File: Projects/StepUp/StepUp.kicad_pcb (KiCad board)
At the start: 4 copper layers, 101 x 81 mm, 149 parts, among them J1 USB_C_Receptacle_USB2.0_16P, J10 Conn_01x02, J11 Conn_01x02, J12 Conn_01x02, J13 Conn_01x02, J14 Conn_02x03_Odd_Even, J2 Conn_01x02, J3 Conn_02x03_Odd_Even, J4 Conn_02x06_Odd_Even, J5 Conn_01x01_Pin, J6 Conn_01x01_Pin, J7 TBLH10-350-04BK, J8 Conn_01x01_Pin, J9 Conn_01x02, Q1 BSS84, Q2 2N7002, Q3 PMF170XP,115, Q4 BSS83P, Q5 BSS83P, SW1 FSM8JSMASTR, SW2 FSM8JSMASTR, SW3 FSM8JSMASTR, U1 USBLC6-2SC6, U2 W25Q128JVS, U3 RP2040, U4 TMC2300-LA, U5 NCP1117-3.3_SOT223, U6 MCP73832T-2ACI_OT, U7 MIC2253, Y1 ABM8-272-T3

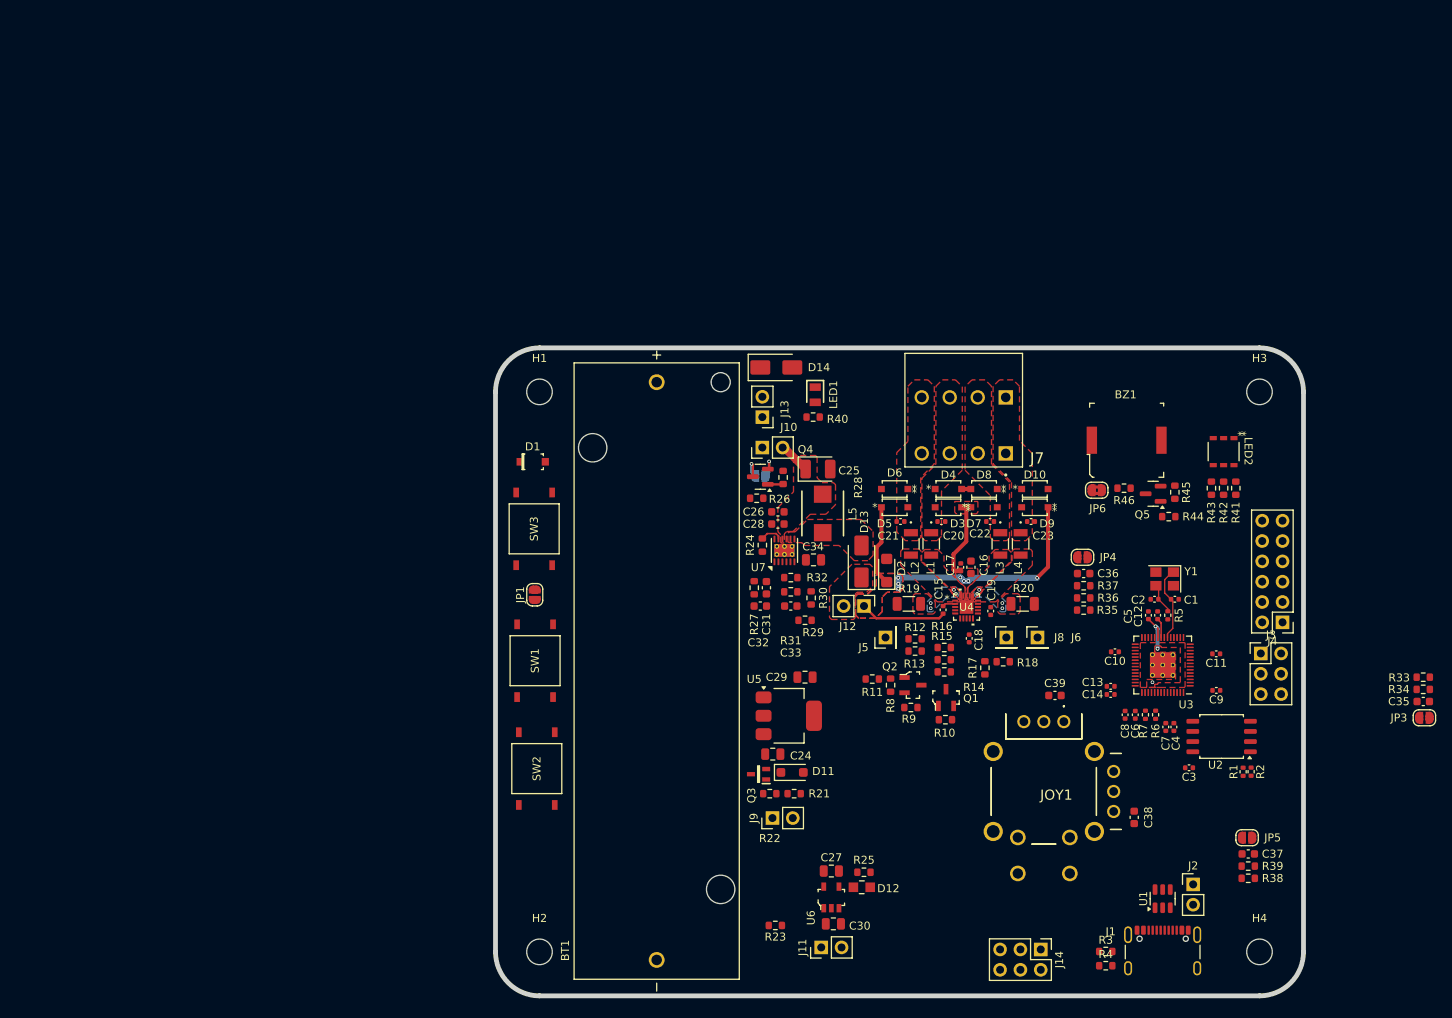
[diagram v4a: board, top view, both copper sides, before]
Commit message: feat(layout): DRC ongoing, layout nearly complete
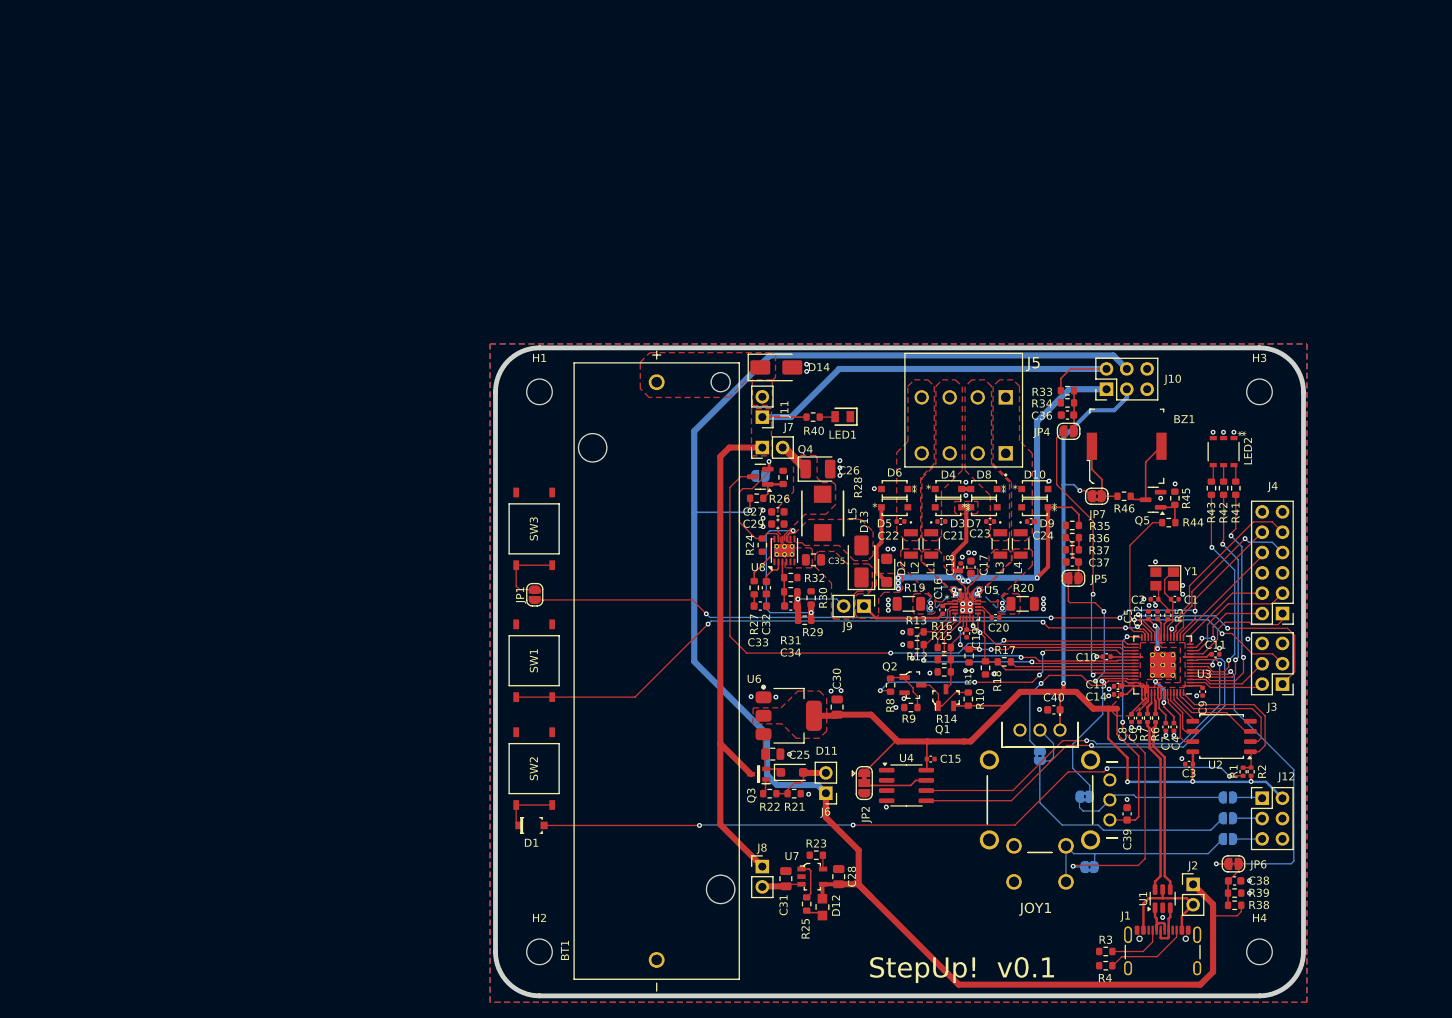
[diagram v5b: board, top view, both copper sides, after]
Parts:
- removed the J5 at (133.2, 100.7)
- removed the J6 at (152.2, 100.7)
- removed the J8 at (148.3, 100.7)
- added C15: 100n, Capacitor_SMD:C_0402_1005Metric, F.Cu at (138.9, 115.9)
- added J10: Conn_02x03_Odd_Even, Connector_PinHeader_2.54mm:PinHeader_2x03_P2.54mm_Vertical, F.Cu at (160.9, 69.7)
- added JP10: SolderJumper_2_Open, Jumper:SolderJumper-2_P1.3mm_Open_RoundedPad1.0x1.5mm, B.Cu at (176.1, 120.7)
- added JP11: SolderJumper_2_Open, Jumper:SolderJumper-2_P1.3mm_Open_RoundedPad1.0x1.5mm, B.Cu at (176.1, 123.3)
- added JP12: SolderJumper_2_Open, Jumper:SolderJumper-2_P1.3mm_Open_RoundedPad1.0x1.5mm, B.Cu at (176.1, 125.9)
- added JP13: SolderJumper_2_Bridged, Jumper:SolderJumper-2_P1.3mm_Bridged2Bar_RoundedPad1.0x1.5mm, B.Cu at (158.8, 129.4)
- added JP2: SolderJumper_3_Open, Jumper:SolderJumper-3_P1.3mm_Bridged12_RoundedPad1.0x1.5mm, F.Cu at (130.6, 118.9)
- added JP8: SolderJumper_2_Bridged, Jumper:SolderJumper-2_P1.3mm_Bridged2Bar_RoundedPad1.0x1.5mm, B.Cu at (152.6, 115.5)
- added JP9: SolderJumper_2_Bridged, Jumper:SolderJumper-2_P1.3mm_Bridged2Bar_RoundedPad1.0x1.5mm, B.Cu at (158.2, 120.6)
- added U4: FM24CL16B, Package_SO:SOIC-8_3.9x4.9mm_P1.27mm, F.Cu at (135.9, 119.2)
- moved C36 57.1 mm to (156.0, 72.9)
- moved JP4 57.1 mm to (156.1, 74.9)
- moved R33 57.1 mm to (156.0, 69.9)
- moved R34 57.1 mm to (156.0, 71.4)
- moved D1 45.5 mm to (89.0, 124.2)
- moved J12 33.5 mm to (180.3, 120.8), turned to 0 degrees
- moved J8 12.5 mm to (117.9, 129.3), turned to 0 degrees
- moved R11 12.4 mm to (143.7, 103.0), turned to -90 degrees
- moved R35 10.7 mm to (156.6, 86.7), turned to 0 degrees
- moved R23 10.2 mm to (124.6, 127.9), turned to 0 degrees
- moved C31 8.19 mm to (120.8, 130.9), turned to 90 degrees
- moved R25 8.19 mm to (123.4, 134.0), turned to -90 degrees
- moved R36 7.67 mm to (156.6, 88.2), turned to 0 degrees
- moved J6 7.36 mm to (125.8, 120.2), turned to 180 degrees
- moved D12 5.51 mm to (125.4, 134.4), turned to -90 degrees
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- renumbered C15 to C16, C16 to C17, C17 to C18, C18 to C19, C19 to C20, C20 to C21, C21 to C22, C22 to C23, C23 to C24, C24 to C25, C25 to C26, C26 to C27, C27 to C28, C28 to C29, C29 to C30, C30 to C31, C31 to C32, C32 to C33, C33 to C34, C34 to C35, C35 to C36, C36 to C37, C37 to C38, C38 to C39, C39 to C40, J13 to J11, J14 to J12, J7 to J5, J9 to J6, J10 to J7, J11 to J8, J12 to J9, JP2 to JP3, JP3 to JP4, JP4 to JP5, JP5 to JP6, JP6 to JP7, U4 to U5, U5 to U6, U6 to U7, U7 to U8
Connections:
- J12 pad 1: JOYSTSICK_AXIS_V -> Net-(J12-Pin_1)
- J12 pad 3: JOYSTSICK_AXIS_H -> Net-(J12-Pin_3)
- J12 pad 5: JOYSTSICK_BUTTON -> Net-(J12-Pin_5)
- J4 pad 1: /MCU/GPIO6 -> /MCU/GPIO8
- J4 pad 10: GND -> /MCU/GPIO13
- J4 pad 3: /MCU/GPIO7 -> /MCU/GPIO9
- J4 pad 5: /MCU/GPIO8 -> GND
- J4 pad 6: /MCU/GPIO12 -> GND
- J4 pad 7: /MCU/GPIO9 -> /MCU/GPIO14
- J4 pad 8: /MCU/GPIO13 -> /MCU/GPIO12
- J4 pad 9: /MCU/GPIO16 -> /MCU/GPIO15
- JOY1 pad 12: JOYSTSICK_AXIS_V -> /User Input/JOYSTICK_AXIS_V
- JOY1 pad 2: JOYSTSICK_AXIS_H -> /User Input/JOYSTICK_AXIS_H
- JOY1 pad B1: JOYSTSICK_BUTTON -> /User Input/JOYSTICK_BUTTON
- JOY1 pad D1: JOYSTSICK_BUTTON -> /User Input/JOYSTICK_BUTTON
- U3 pad 17: TMC_EN -> /MCU/GPIO14
- U3 pad 18: ~{TMC_STBDY} -> /MCU/GPIO15
- U3 pad 27: /MCU/GPIO16 -> BUZZER
- U3 pad 28: BUZZER -> JOY_MCU_BTN
- U3 pad 29: VUSB_MONITOR -> MCU_BOOST_EN
- U3 pad 30: MCU_BOOST_EN -> TMC_DIAG
- U3 pad 31: TMC_DIAG -> TMC_EN
- U3 pad 32: VUSB_MONITOR -> ~{TMC_STBDY}
- U3 pad 34: JOYSTSICK_BUTTON -> TMC_DIR
- U3 pad 35: LED_RED -> TMC_STEP
- U3 pad 36: LED_GREEN -> TMC_UART_TX
- U3 pad 37: LED_BLUE -> TMC_UART_RX
- U3 pad 38: JOYSTSICK_AXIS_V -> VBAT_MONITOR
- U3 pad 39: JOYSTSICK_AXIS_H -> VMOTOR_MONITOR
- U3 pad 4: TMC_STEP -> LED_RED
- U3 pad 40: VBAT_MONITOR -> JOY_AXIS_MCU_V
- U3 pad 41: VMOTOR_MONITOR -> JOY_AXIS_MCU_H
- U3 pad 5: TMC_DIR -> LED_GREEN
- U3 pad 6: TMC_UART_TX -> VUSB_MONITOR
- U3 pad 7: TMC_UART_RX -> LED_BLUE
- U3 pad 8: /MCU/GPIO6 -> /MCU/EEPROM_SDA
- U3 pad 9: /MCU/GPIO7 -> /MCU/EEPROM_SCL
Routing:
- net V_USB: track 0.00 -> 210.5 mm, vias 0 -> 1
- net +3V3: track 2.48 -> 196.0 mm, vias 0 -> 5
- net Vbat: track 0.00 -> 123.3 mm
- net /MCU/GPIO13: track 0.00 -> 101.5 mm, vias 0 -> 4
- net /MCU/~{USB_BOOT}: track 0.00 -> 90.9 mm, vias 0 -> 4
- net /MCU/RUN: track 0.00 -> 84.1 mm, vias 0 -> 4
- net MCU_BOOST_EN: track 3.52 -> 74.5 mm, vias 1 -> 2
- net /MCU/EEPROM_SDA: track 0.00 -> 53.3 mm, vias 0 -> 2
- net /MCU/EEPROM_SCL: track 0.00 -> 50.5 mm, vias 0 -> 2
- net VUSB_MONITOR: track 0.00 -> 43.8 mm, vias 0 -> 2
- net JOY_MCU_BTN: track 0.00 -> 42.1 mm, vias 0 -> 3
- net VBAT_MONITOR: track 0.00 -> 38.2 mm, vias 0 -> 2
- net TMC_DIR: track 0.00 -> 38.1 mm, vias 0 -> 2
- net ~{TMC_STBDY}: track 0.00 -> 36.9 mm, vias 0 -> 4
- net /User Input/JOYSTICK_AXIS_H: track 0.00 -> 35.8 mm
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- added copper zone on B.Cu, net GND
- added copper zone on F.Cu, net GND
- added copper zone on F.Cu, net Net-(D14-K)
- added copper zone on F.Cu, net Vbat
- removed copper zone on B.Cu, net VMotor
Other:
- board text added: "StepUp! v0.1"

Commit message: feat(StepUp): Release v0.1
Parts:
- added R8: 10kR, Resistor_SMD:R_0603_1608Metric, F.Cu at (82.4, 78.1)
- added R9: 10kR, Resistor_SMD:R_0603_1608Metric, F.Cu at (84.6, 79.3)
- C1, C2: value 15p -> 15pF
- C10, C11, C12, C13, C3, C4, C5, C7, C9: value 100n -> 100nF
- C14: renamed from C15; value 100n -> 100nF
- C15: renamed from C14; value 100n -> 100nF
- C25: value 10uF -> 1uF
- C28, C31: value 4.7u -> 4.7uF
- C6, C8: value 1u -> 1uF
- H1, H2, H3, H4: footprint MountingHole:MountingHole_3.2mm_M3 -> MountingHole:MountingHole_3.2mm_M3_DIN965_Pad
- U5: footprint Ultra_librarian_footprints:QFN20_3x3_TRI -> Ultra_librarian_footprints:QFN20_3x3_TRI-M
- U6: value NCP1117-3.3_SOT223 -> LDL1117S33R
- moved D1 72.5 mm to (29.2, 83.2)
- moved C16 72.1 mm to (81.0, 56.3)
- moved C1 72.1 mm to (110.2, 54.9)
- moved C14 72.1 mm to (79.6, 74.9)
- moved C15 72.1 mm to (103.0, 66.8)
- moved C30 72.1 mm to (67.9, 68.4)
- moved C9 72.1 mm to (113.6, 66.5)
- moved D4 72.1 mm to (81.9, 41.2)
- moved D6 72.1 mm to (75.1, 41.2)
- moved J2 72.1 mm to (112.4, 90.6)
- moved JP10 72.1 mm to (116.8, 79.7)
- moved JP12 72.1 mm to (116.8, 84.9)
- moved R1 72.1 mm to (118.7, 76.5)
- moved R3 72.1 mm to (101.5, 99.0)
- moved BT1 72.1 mm to (45.4, 63.9)
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- renumbered R8 to R10, R9 to R11, R10 to R12, R11 to R13, R12 to R14, R13 to R15, R14 to R16, R15 to R17, R16 to R18, R17 to R19, R18 to R20, R19 to R21, R20 to R22, R21 to R23, R22 to R24, R23 to R25, R24 to R26, R25 to R27, R26 to R28, R27 to R29, R28 to R30, R29 to R31, R30 to R32, R31 to R33, R32 to R34, R33 to R35, R34 to R36, R35 to R37, R36 to R38, R37 to R39, R38 to R40, R39 to R41, R40 to R42, R41 to R43, R42 to R44, R43 to R45, R44 to R46, R45 to R47, R46 to R48
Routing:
- net +3V3: track 196.0 -> 206.4 mm
- net MCU_BOOST_EN: track 74.5 -> 77.2 mm, vias 2 -> 3
- net GND: track 4.98 -> 6.78 mm, vias 71 -> 172
- net USB_D+_IN: track 5.82 -> 7.57 mm
- net USB_D-_IN: track 5.43 -> 4.70 mm
- net /MCU/~{USB_BOOT}: track 90.9 -> 91.4 mm
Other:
- board text added: "0"
- board text added: "0 mm"
- board text added: "0.01 mm"
- board text added: "0.02"
- board text added: "0.035 mm"
- board text added: "0.1500 mm / 0.1500 mm"
- board text added: "0.1785 mm"
- board text added: "0.3000 mm"
- board text added: "1"
- board text added: "1 x 18650 cell"
- board text added: "1.03 mm"
- board text added: "1.5470 mm"
- board text added: "101.0000 mm x 81.0000 mm"
- board text added: "3.3"
- board text added: "3V3"
- board text added: "4"
- board text added: "4.56"
- board text added: "4.6"
- board text added: "A2 A1"
- board text added: "B.Cu"
- board text added: "B.Mask"
- board text added: "B.Paste"
- board text added: "B.Silkscreen"
- board text added: "B1 B2"
- board text added: "BOARD CHARACTERISTICS"
- board text added: "Board Thickness:"
- board text added: "Board overall dimensions:"
- board text added: "Bottom Silk Screen"
- board text added: "Bottom Solder Mask"
- board text added: "Bottom Solder Paste"
- board text added: "Castellated pads:"
- board text added: "Color"
- board text added: "Copper Finish:"
- board text added: "Copper Layer Count:"
- board text added: "Dielectric"
- board text added: "Edge card connectors:"
- board text added: "Epsilon R"
- board text added: "F.Cu"
- board text added: "F.Mask"
- board text added: "F.Paste"
- board text added: "F.Silkscreen"
- board text added: "FR4"
- board text added: "G G 13 15 12 14 G G 11 9 10 8"
- board text added: "G G RX SWD TX SCK"
- board text added: "GPIO"
- board text added: "Green"
- board text added: "HAL lead-free"
- board text added: "Impedance Control:"
- board text added: "In1.Cu"
- board text added: "In2.Cu"
- board text added: "Layer Name"
- board text added: "Loss Tangent"
- board text added: "Material"
- board text added: "Min hole diameter:"
- board text added: "Min track/spacing:"
- board text added: "No"
- board text added: "Not specified"
- board text added: "PROGRAM"
- board text added: "Plated Board Edge:"
- board text added: "RESET"
- board text added: "SJFOM"
- board text added: "Status LED"
- board text added: "Thickness (mm)"
- board text added: "Top Silk Screen"
- board text added: "Top Solder Mask"
- board text added: "Top Solder Paste"
- board text added: "Type"
- board text added: "USER"
- board text added: "Vbat OK"
- board text added: "Vbat Vusb G Vmtr 3V3 G"
- board text added: "White"
- board text added: "X"
- board text added: "Y"
- board text added: "Yes"
- board text added: "copper"
- board text added: "core"
- board text added: "prepreg"
